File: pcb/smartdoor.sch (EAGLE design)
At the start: 5 parts

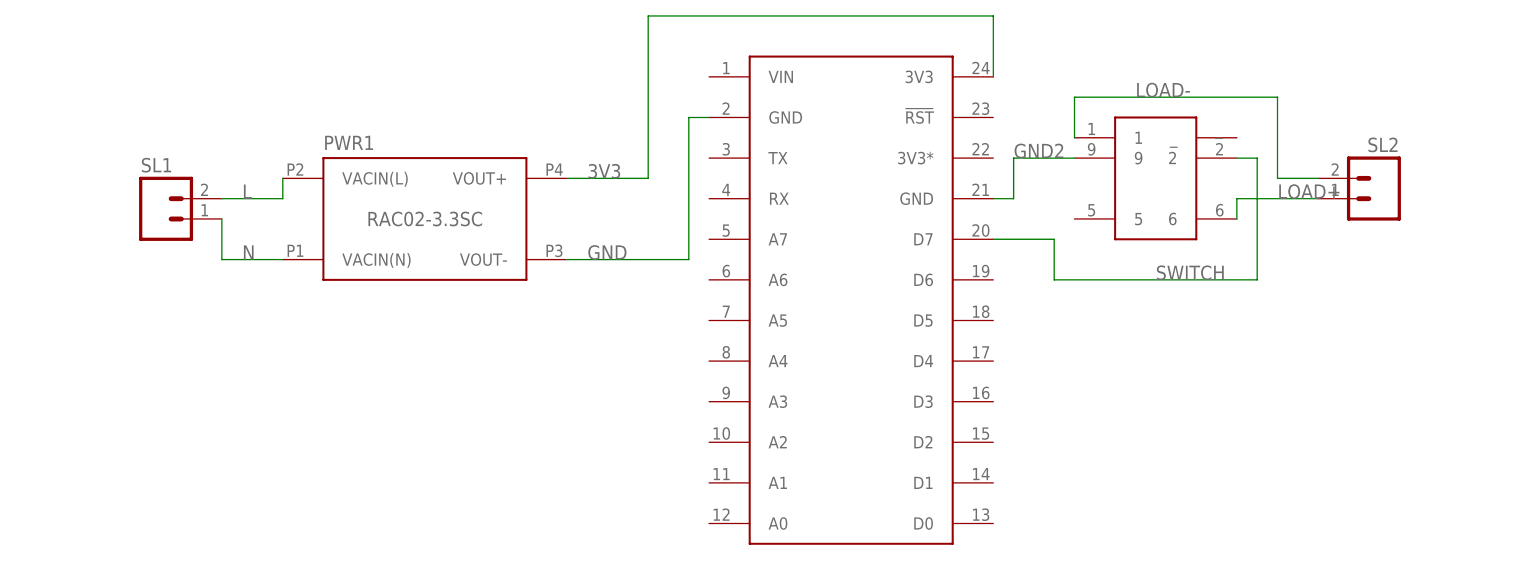
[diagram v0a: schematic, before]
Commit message: new pcb board layout, renamed files
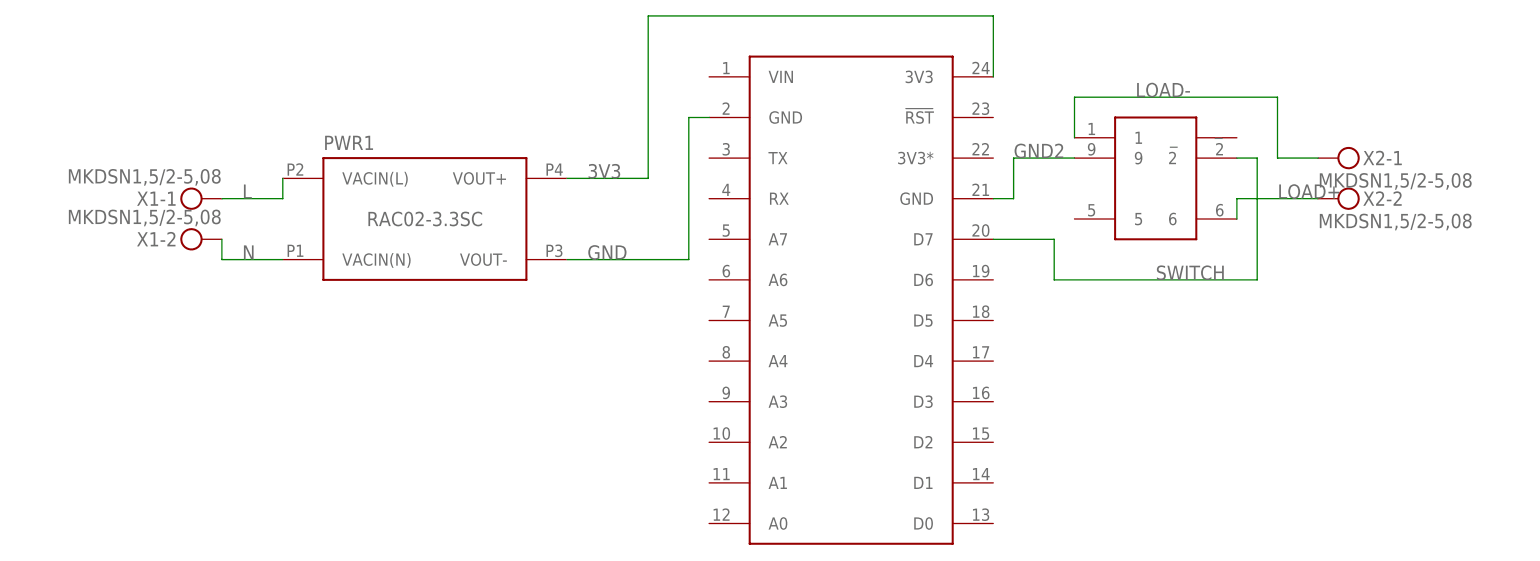
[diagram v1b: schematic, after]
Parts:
- removed SL1, SL2: (no value), con-amp-quick:M02
- added X1, X2: MKDSN1,5/2-5,08, con-phoenix-508:MKDSN1,5/2-5,08
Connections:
- net L: now also X1-1.KL; no longer SL1.2
- net LOAD+: now also X2-2.KL; no longer SL2.1
- net LOAD-: now also X2-1.KL; no longer SL2.2
- net N: now also X1-2.KL; no longer SL1.1
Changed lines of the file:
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@@
 <part name="RELAY1" library="Zettler" deviceset="AZ9571" device="AZ9571"/>
 <part name="FRAME1" library="frames" library_urn="urn:adsk.eagle:library:229" deviceset="DINA5_L" device=""/>
-<part name="SL1" library="con-amp-quick" library_urn="urn:adsk.eagle:library:125" deviceset="M02" device=""/>
-<part name="SL2" library="con-amp-quick" library_urn="urn:adsk.eagle:library:125" deviceset="M02" device=""/>
+<part name="X1" library="con-phoenix-508" library_urn="urn:adsk.eagle:library:176" deviceset="MKDSN1,5/2-5,08" device=""/>
+<part name="X2" library="con-phoenix-508" library_urn="urn:adsk.eagle:library:176" deviceset="MKDSN1,5/2-5,08" device=""/>
 </parts>
 <sheets>
@@
 <instance part="RELAY1" gate="G$1" x="142.24" y="83.82"/>
 <instance part="FRAME1" gate="G$1" x="0" y="0"/>
-<instance part="SL1" gate="G$1" x="17.78" y="78.74"/>
-<instance part="SL2" gate="G$1" x="170.18" y="81.28" rot="MR0"/>
+<instance part="X1" gate="-1" x="22.86" y="81.28" rot="R180"/>
+<instance part="X1" gate="-2" x="22.86" y="76.2" rot="R180"/>
+<instance part="X2" gate="-1" x="165.1" y="86.36"/>
+<instance part="X2" gate="-2" x="165.1" y="81.28"/>
 </instances>
 <busses>
@@
 <segment>
 <pinref part="PWR1" gate="_MODULE" pin="VACIN(N)"/>
-<pinref part="SL1" gate="G$1" pin="1"/>
 <wire x1="33.02" y1="73.66" x2="25.4" y2="73.66" width="0.1524" layer="91"/>
-<wire x1="25.4" y1="73.66" x2="25.4" y2="78.74" width="0.1524" layer="91"/>
 <label x="27.94" y="73.66" size="1.778" layer="95"/>
+<pinref part="X1" gate="-2" pin="KL"/>
+<wire x1="25.4" y1="76.2" x2="25.4" y2="73.66" width="0.1524" layer="91"/>
 </segment>
 </net>
 <net name="L" class="0">
 <segment>
-<pinref part="SL1" gate="G$1" pin="2"/>
 <pinref part="PWR1" gate="_MODULE" pin="VACIN(L)"/>
 <wire x1="25.4" y1="81.28" x2="33.02" y2="81.28" width="0.1524" layer="91"/>
 <wire x1="33.02" y1="81.28" x2="33.02" y2="83.82" width="0.1524" layer="91"/>
 <label x="27.94" y="81.28" size="1.778" layer="95"/>
+<pinref part="X1" gate="-1" pin="KL"/>
 </segment>
 </net>
@@
 <net name="LOAD+" class="0">
 <segment>
-<pinref part="SL2" gate="G$1" pin="1"/>
 <pinref part="RELAY1" gate="G$1" pin="6"/>
 <wire x1="162.56" y1="81.28" x2="152.4" y2="81.28" width="0.1524" layer="91"/>
 <wire x1="152.4" y1="81.28" x2="152.4" y2="78.74" width="0.1524" layer="91"/>
 <label x="157.48" y="81.28" size="1.778" layer="95"/>
+<pinref part="X2" gate="-2" pin="KL"/>
 </segment>
 </net>
 <net name="LOAD-" class="0">
 <segment>
-<pinref part="SL2" gate="G$1" pin="2"/>
-<wire x1="162.56" y1="83.82" x2="157.48" y2="83.82" width="0.1524" layer="91"/>
-<wire x1="157.48" y1="83.82" x2="157.48" y2="93.98" width="0.1524" layer="91"/>
+<wire x1="162.56" y1="86.36" x2="157.48" y2="86.36" width="0.1524" layer="91"/>
+<wire x1="157.48" y1="86.36" x2="157.48" y2="93.98" width="0.1524" layer="91"/>
 <pinref part="RELAY1" gate="G$1" pin="1"/>
 <wire x1="157.48" y1="93.98" x2="132.08" y2="93.98" width="0.1524" layer="91"/>
 <wire x1="132.08" y1="93.98" x2="132.08" y2="88.9" width="0.1524" layer="91"/>
 <label x="139.7" y="93.98" size="1.778" layer="95"/>
+<pinref part="X2" gate="-1" pin="KL"/>
 </segment>
 </net>

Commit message: defined net classes and GND pins on relay, new board layout
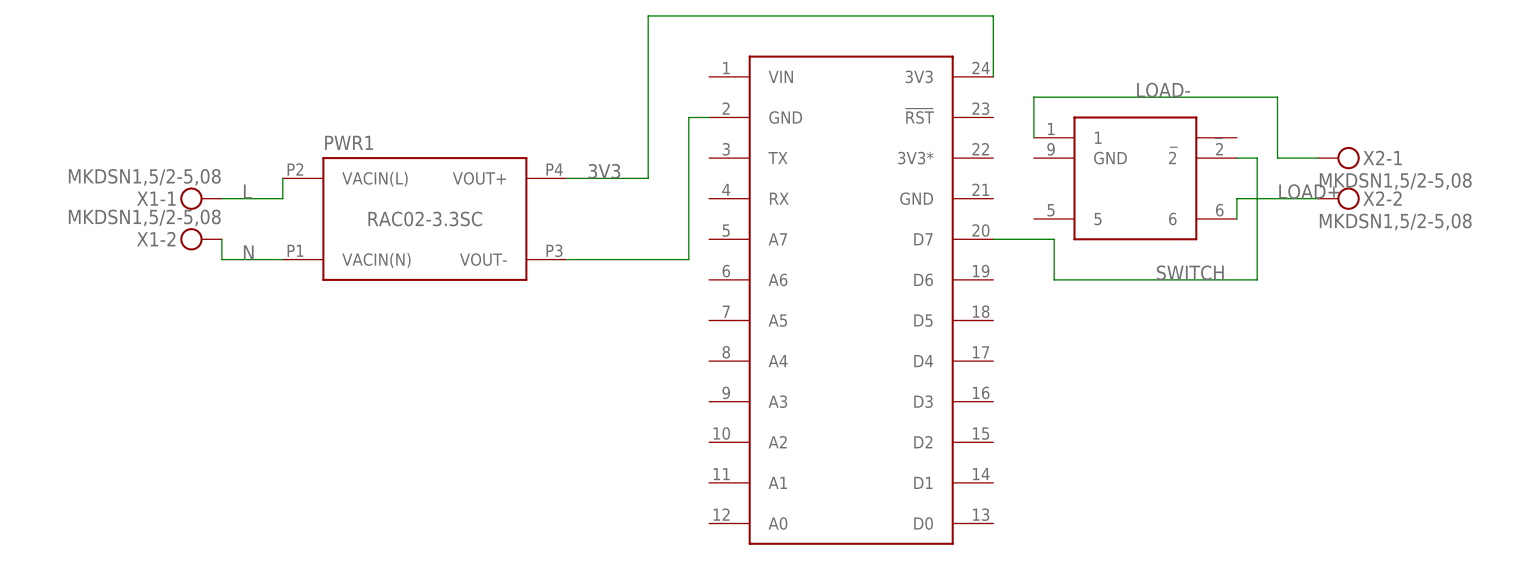
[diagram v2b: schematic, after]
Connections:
- net GND renamed N$1
- removed net GND2: CORE.GND@21, RELAY1.9
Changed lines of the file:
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@@
 </variantdefs>
 <classes>
-<class number="0" name="default" width="0" drill="0">
+<class number="0" name="default" width="0.6096" drill="0.6096">
+<clearance class="0" value="0.6096"/>
 </class>
 </classes>
@@
 <instance part="CORE" gate="G$1" x="104.14" y="68.58"/>
 <instance part="PWR1" gate="_MODULE" x="50.8" y="78.74"/>
-<instance part="RELAY1" gate="G$1" x="142.24" y="83.82"/>
+<instance part="RELAY1" gate="G$1" x="139.7" y="83.82"/>
 <instance part="FRAME1" gate="G$1" x="0" y="0"/>
 <instance part="X1" gate="-1" x="22.86" y="81.28" rot="R180"/>
@@
 </segment>
 </net>
-<net name="GND" class="0">
-<segment>
-<pinref part="PWR1" gate="_MODULE" pin="VOUT-"/>
-<wire x1="68.58" y1="73.66" x2="83.82" y2="73.66" width="0.1524" layer="91"/>
-<wire x1="83.82" y1="73.66" x2="83.82" y2="91.44" width="0.1524" layer="91"/>
-<pinref part="CORE" gate="G$1" pin="GND@2"/>
-<wire x1="83.82" y1="91.44" x2="86.36" y2="91.44" width="0.1524" layer="91"/>
-<label x="71.12" y="73.66" size="1.778" layer="95"/>
-</segment>
-</net>
 <net name="LOAD+" class="0">
 <segment>
@@
 <wire x1="157.48" y1="86.36" x2="157.48" y2="93.98" width="0.1524" layer="91"/>
 <pinref part="RELAY1" gate="G$1" pin="1"/>
-<wire x1="157.48" y1="93.98" x2="132.08" y2="93.98" width="0.1524" layer="91"/>
-<wire x1="132.08" y1="93.98" x2="132.08" y2="88.9" width="0.1524" layer="91"/>
+<wire x1="157.48" y1="93.98" x2="127" y2="93.98" width="0.1524" layer="91"/>
+<wire x1="127" y1="93.98" x2="127" y2="88.9" width="0.1524" layer="91"/>
 <label x="139.7" y="93.98" size="1.778" layer="95"/>
 <pinref part="X2" gate="-1" pin="KL"/>
-</segment>
-</net>
-<net name="GND2" class="0">
-<segment>
-<pinref part="RELAY1" gate="G$1" pin="9"/>
-<wire x1="132.08" y1="86.36" x2="124.46" y2="86.36" width="0.1524" layer="91"/>
-<wire x1="124.46" y1="86.36" x2="124.46" y2="81.28" width="0.1524" layer="91"/>
-<pinref part="CORE" gate="G$1" pin="GND@21"/>
-<wire x1="124.46" y1="81.28" x2="121.92" y2="81.28" width="0.1524" layer="91"/>
-<label x="124.46" y="86.36" size="1.778" layer="95"/>
 </segment>
 </net>
@@
 </segment>
 </net>
+<net name="N$1" class="0">
+<segment>
+<pinref part="PWR1" gate="_MODULE" pin="VOUT-"/>
+<wire x1="68.58" y1="73.66" x2="83.82" y2="73.66" width="0.1524" layer="91"/>
+<wire x1="83.82" y1="73.66" x2="83.82" y2="91.44" width="0.1524" layer="91"/>
+<pinref part="CORE" gate="G$1" pin="GND@2"/>
+<wire x1="83.82" y1="91.44" x2="86.36" y2="91.44" width="0.1524" layer="91"/>
+</segment>
+</net>

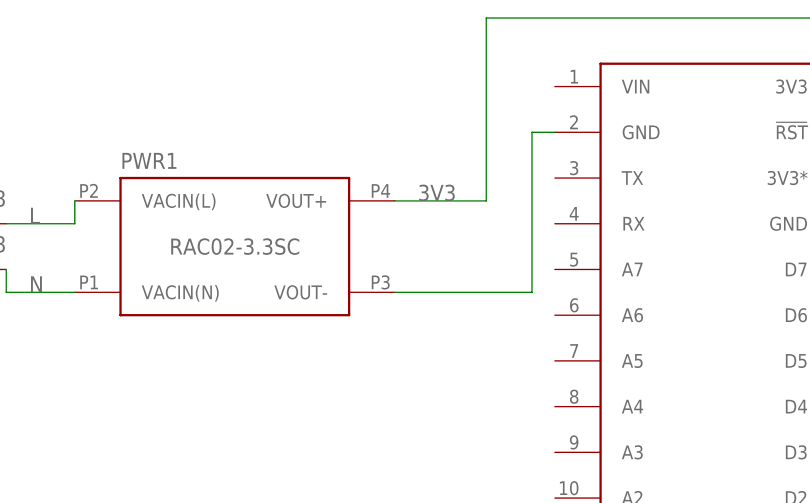
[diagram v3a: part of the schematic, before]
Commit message: fixed connecting V- of recom with GND mass, updated larger pads for zettler relay in board
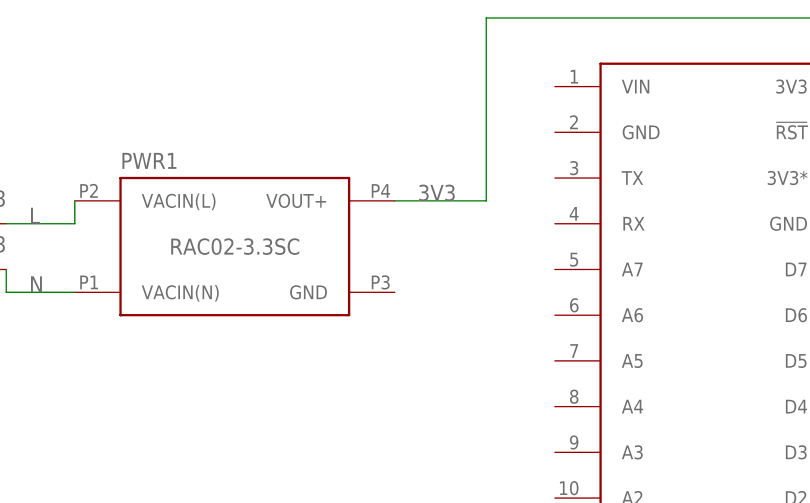
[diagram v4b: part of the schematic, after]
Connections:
- removed net N$1: CORE.GND@2, PWR1.VOUT-
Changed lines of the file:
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@@
 <?xml version="1.0" encoding="utf-8"?>
 <!DOCTYPE eagle SYSTEM "eagle.dtd">
-<eagle version="8.2.0">
+<eagle version="8.2.1">
 <drawing>
 <settings>
@@
 </segment>
 </net>
-<net name="N$1" class="0">
-<segment>
-<pinref part="PWR1" gate="_MODULE" pin="VOUT-"/>
-<wire x1="68.58" y1="73.66" x2="83.82" y2="73.66" width="0.1524" layer="91"/>
-<wire x1="83.82" y1="73.66" x2="83.82" y2="91.44" width="0.1524" layer="91"/>
-<pinref part="CORE" gate="G$1" pin="GND@2"/>
-<wire x1="83.82" y1="91.44" x2="86.36" y2="91.44" width="0.1524" layer="91"/>
-</segment>
-</net>

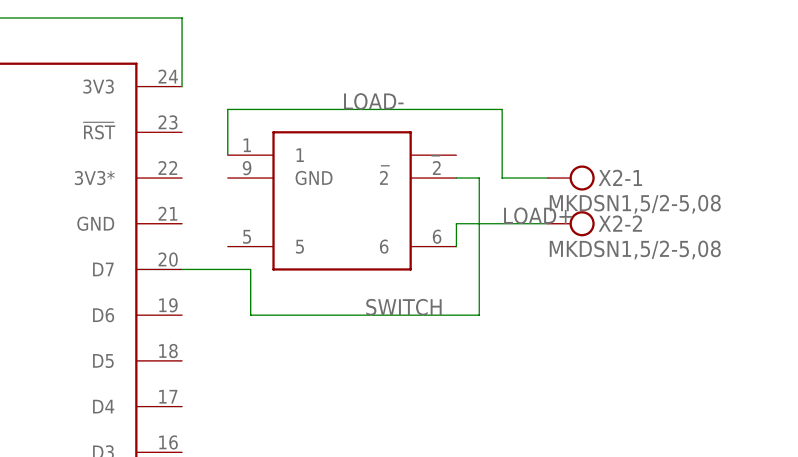
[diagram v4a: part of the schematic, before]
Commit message: fixed mirrored relay
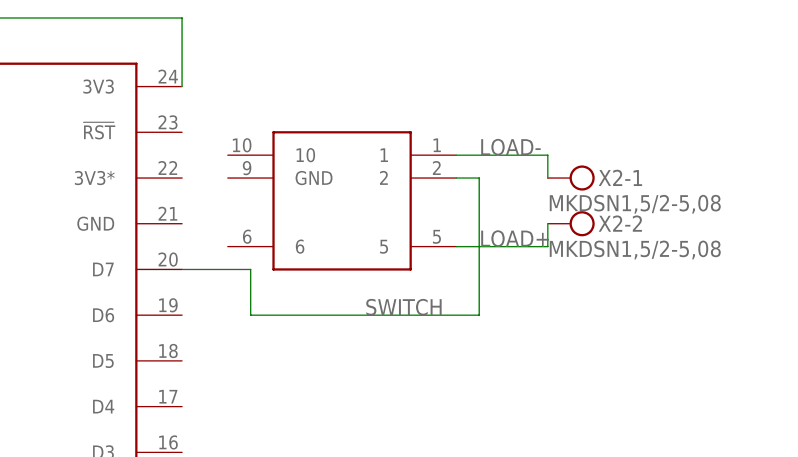
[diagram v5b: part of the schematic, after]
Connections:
- net LOAD+: now also RELAY1.5; no longer RELAY1.6
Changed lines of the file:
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@@
-</segment>
-</net>
-<net name="LOAD+" class="0">
-<segment>
-<pinref part="RELAY1" gate="G$1" pin="6"/>
-<wire x1="162.56" y1="81.28" x2="152.4" y2="81.28" width="0.1524" layer="91"/>
-<wire x1="152.4" y1="81.28" x2="152.4" y2="78.74" width="0.1524" layer="91"/>
-<label x="157.48" y="81.28" size="1.778" layer="95"/>
-<pinref part="X2" gate="-2" pin="KL"/>
-</segment>
-</net>
-<net name="LOAD-" class="0">
-<segment>
-<wire x1="162.56" y1="86.36" x2="157.48" y2="86.36" width="0.1524" layer="91"/>
-<wire x1="157.48" y1="86.36" x2="157.48" y2="93.98" width="0.1524" layer="91"/>
-<pinref part="RELAY1" gate="G$1" pin="1"/>
-<wire x1="157.48" y1="93.98" x2="127" y2="93.98" width="0.1524" layer="91"/>
-<wire x1="127" y1="93.98" x2="127" y2="88.9" width="0.1524" layer="91"/>
-<label x="139.7" y="93.98" size="1.778" layer="95"/>
-<pinref part="X2" gate="-1" pin="KL"/>
 </segment>
 </net>
@@
 </segment>
 </net>
+<net name="LOAD-" class="0">
+<segment>
+<pinref part="RELAY1" gate="G$1" pin="1"/>
+<pinref part="X2" gate="-1" pin="KL"/>
+<wire x1="152.4" y1="88.9" x2="162.56" y2="88.9" width="0.1524" layer="91"/>
+<wire x1="162.56" y1="88.9" x2="162.56" y2="86.36" width="0.1524" layer="91"/>
+<label x="154.94" y="88.9" size="1.778" layer="95"/>
+</segment>
+</net>
+<net name="LOAD+" class="0">
+<segment>
+<pinref part="RELAY1" gate="G$1" pin="5"/>
+<pinref part="X2" gate="-2" pin="KL"/>
+<wire x1="152.4" y1="78.74" x2="162.56" y2="78.74" width="0.1524" layer="91"/>
+<wire x1="162.56" y1="78.74" x2="162.56" y2="81.28" width="0.1524" layer="91"/>
+<label x="154.94" y="78.74" size="1.778" layer="95"/>
+</segment>
+</net>
